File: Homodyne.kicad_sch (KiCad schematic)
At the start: 45 parts, among them J1 5-1814832-1, J4 Conn_01x03_Male 0022232031, U1 LM337_SOT223, U2 LM317DCYR, U3 OPA847xD, U4 LM337_SOT223, U5 LM317DCYR

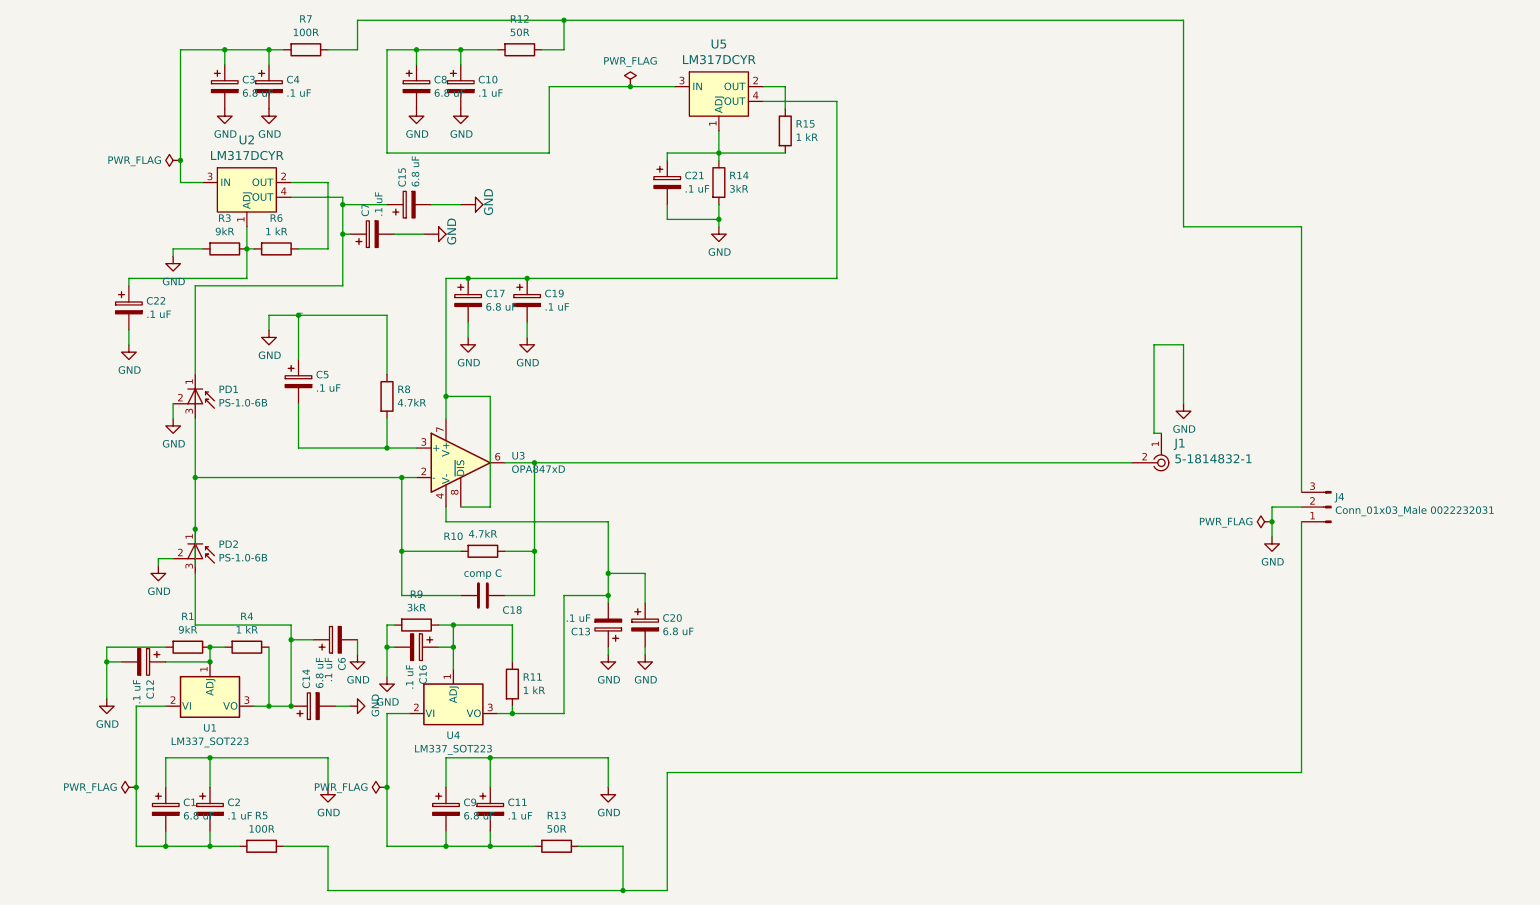
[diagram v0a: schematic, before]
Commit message: Updated the board size to 65x65 mm
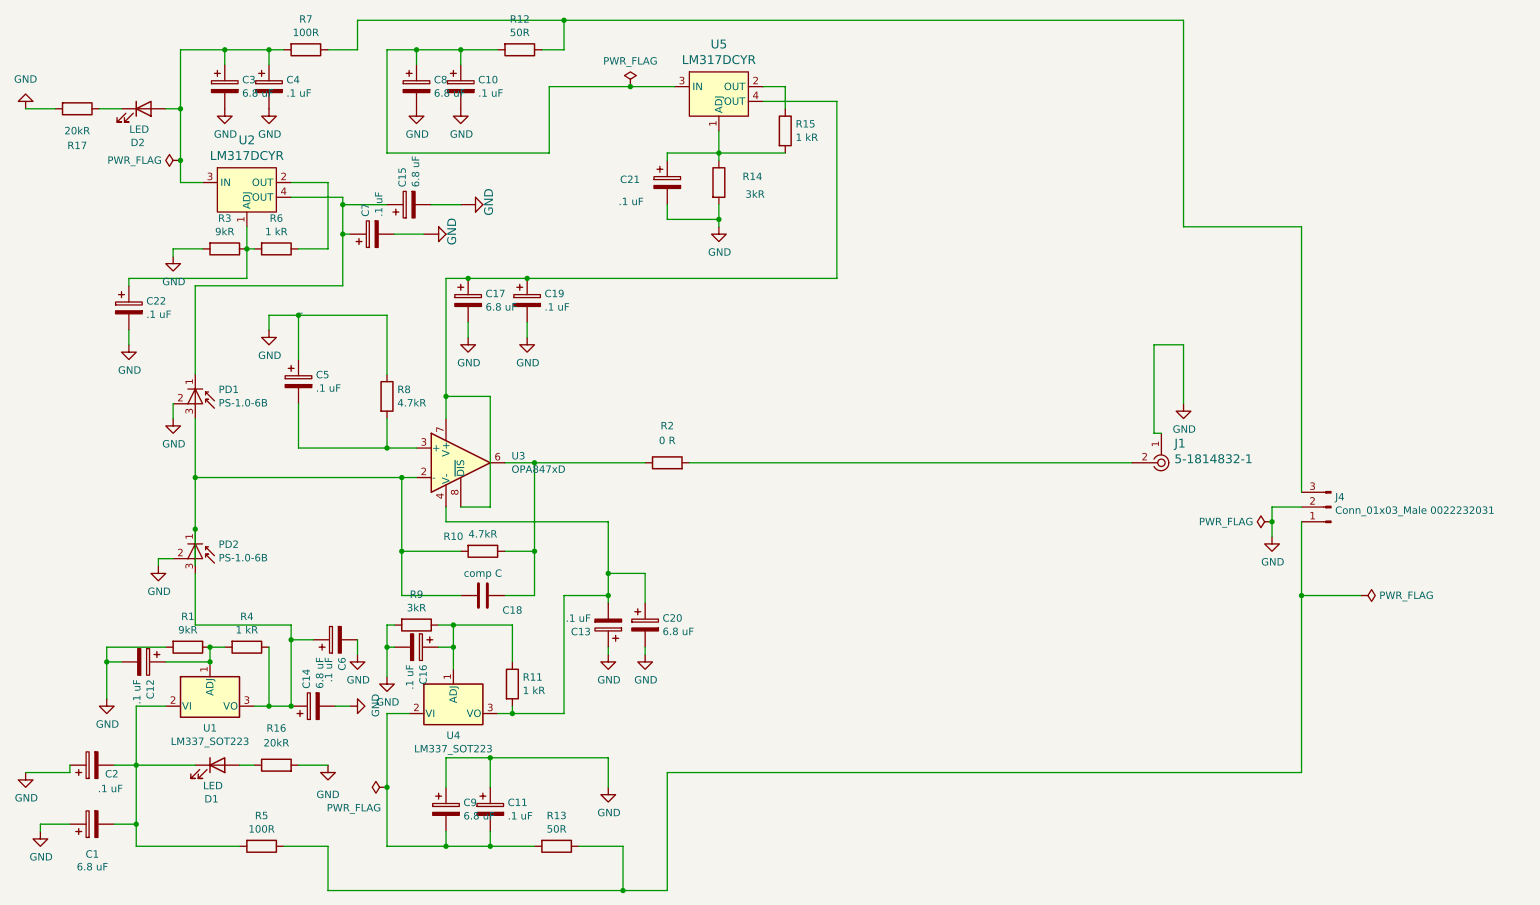
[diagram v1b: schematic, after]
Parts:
- added D1, D2: LED, LED_SMD:LED_1206_3216Metric, symbol Device:LED
- added R16, R17: 20kR, Resistor_SMD:R_1206_3216Metric, symbol Device:R
- added R2: 0 R, Resistor_SMD:R_1206_3216Metric, symbol Device:R
- J4: footprint digikey-footprints:PinHeader_1x3_P2.54_Drill1.1mm -> Connector_PinHeader_2.54mm:PinHeader_1x03_P2.54mm_Vertical
- U2, U5: footprint digikey-footprints:SOT-223-4 -> Package_TO_SOT_SMD:SOT-223
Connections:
- net GND: now also R16.2, R17.2
- net at C3.1, C4.1, R7.2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: now also D2.2 (A)
- net at C1.2, C2.2, R5.2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: now also D1.1 (K)
- net at C18.1, R10.1, U3.6: now also R2.1; no longer J1.2
- new net: J1.2, R2.2
- new net: D1.2 (A), R16.1
- new net: D2.1 (K), R17.1
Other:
- moved on the sheet: C1, C2
